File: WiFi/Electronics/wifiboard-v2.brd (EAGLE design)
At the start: 95.2 x 43.2 mm, 16 parts, among them IC2 7805DT, Q1 FDD8870, X1 MKDSN1,5/2-5,08, X2 MKDSN1,5/2-5,08

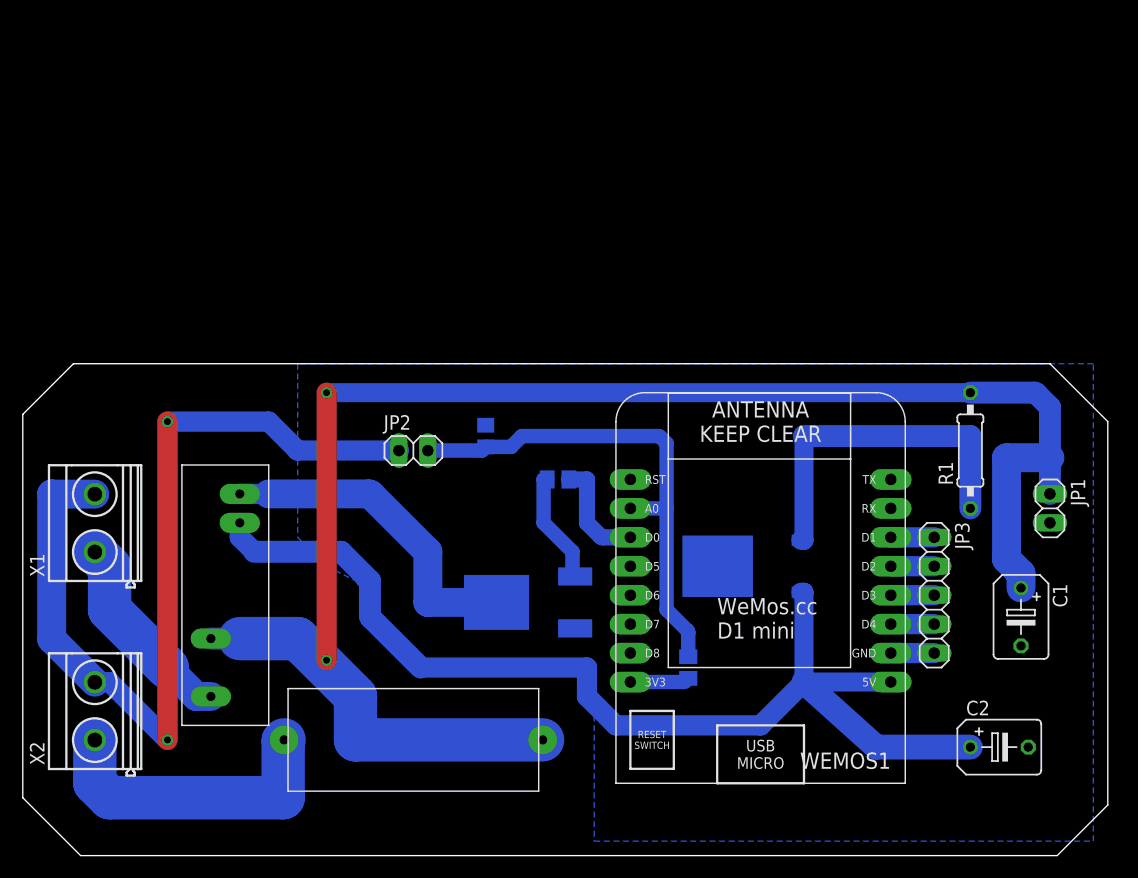
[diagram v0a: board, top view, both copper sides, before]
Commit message: heating.php improved to check that times monotonically increase throughout the day.
Various bits of experimental WiFi electronics added.
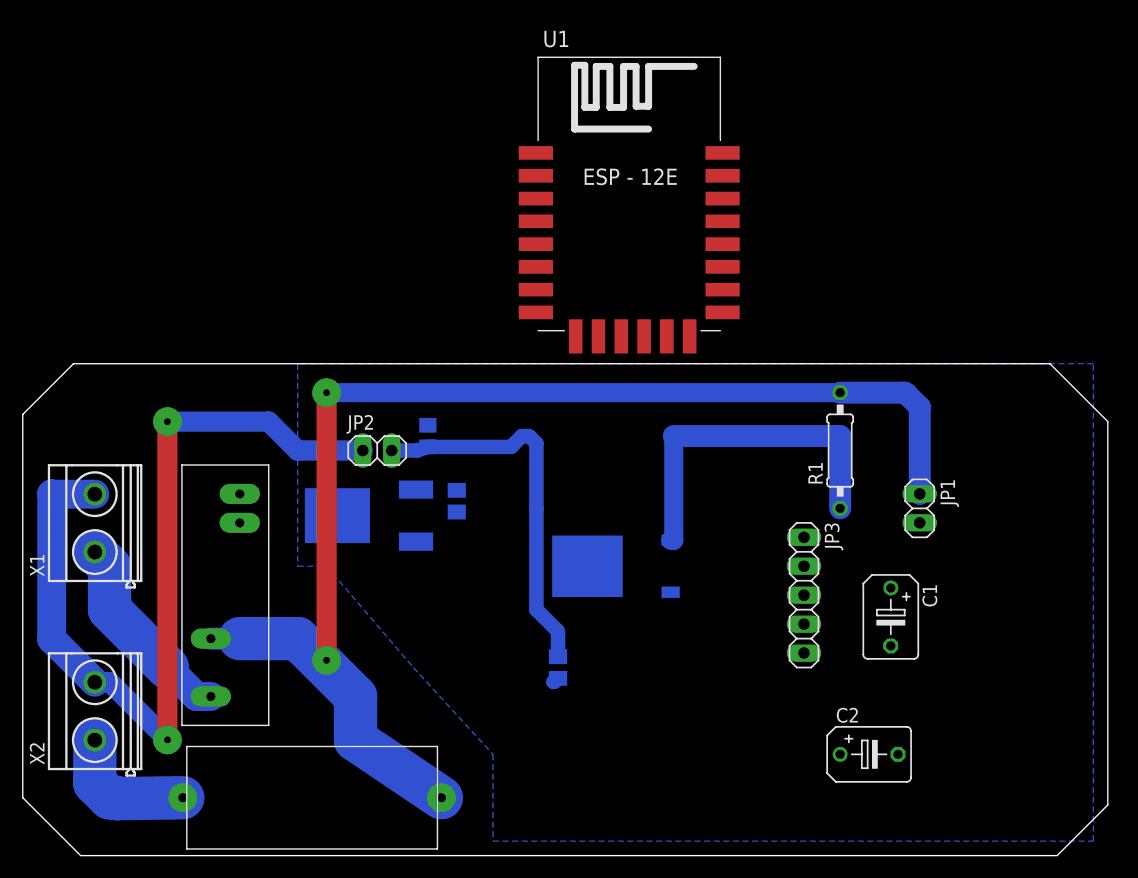
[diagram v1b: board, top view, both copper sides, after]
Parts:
- removed WEMOS1: (no value), esp8266modules:WEMOS-D1-MINI
- added U1: (no value), esp8266modules:ESP12E-SMD
- moved Q1 15.9 mm to (29.2, 28.6)
- moved C2 11.4 mm to (74.3, 7.62)
- moved JP1 11.4 mm to (78.7, 29.2)
- moved JP3 11.4 mm to (68.6, 21.6)
- moved R1 11.4 mm to (71.8, 34.3)
- moved IC2 11.4 mm to (52.1, 24.1)
- moved R2 11.4 mm to (47.0, 15.2)
- moved C1 11.4 mm to (76.2, 19.7)
- moved U$2 10.2 mm to (25.4, 3.81)
- moved R3 9.09 mm to (38.1, 29.8), turned to 270 degrees
- moved C3 5.08 mm to (35.6, 35.6)
- moved JP2 3.18 mm to (31.1, 34.3)
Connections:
- removed net N$11: JP3.4, WEMOS1.D4
- removed net N$13: JP3.3, WEMOS1.D3
- removed net N$14: JP3.2, WEMOS1.D2
- removed net N$15: JP3.1, WEMOS1.D1
- removed net N$3: C3.1, JP2.2, R2.2, WEMOS1.A0
- removed net N$4: R2.1, WEMOS1.3V3
- removed net N$6: R3.2, WEMOS1.D0
- new net +3V3: R2.1
- new net A0: C3.1, JP2.2, R2.2
- new net D0: R3.2
- new net D1: JP3.1
- new net D2: JP3.2
- new net D3: JP3.3
- new net D4: JP3.4
- net +12V: no longer C1.+
- net +5V: no longer WEMOS1.5V
- net GND: no longer WEMOS1.GND
- net N$2: now also C1.+
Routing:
- net +5V: track 95.1 -> 0.00 mm
- net N$3: track 44.4 -> 0.00 mm
- net +12V: track 148.4 -> 113.8 mm
- net A0: track 0.00 -> 32.9 mm
- net N$7: track 29.1 -> 0.00 mm
- net N$12: track 25.9 -> 12.1 mm
- net N$5: track 9.98 -> 0.00 mm
- net N$6: track 9.72 -> 0.00 mm
- net GND: track 83.5 -> 76.5 mm
- net N$4: track 5.20 -> 0.00 mm
- net N$15: track 3.81 -> 0.00 mm
- net N$14: track 3.81 -> 0.00 mm
- net N$13: track 3.81 -> 0.00 mm
- net N$11: track 3.81 -> 0.00 mm
- net +3V3: track 0.00 -> 0.54 mm

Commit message: Simple web monitoring added to the thermostat program.
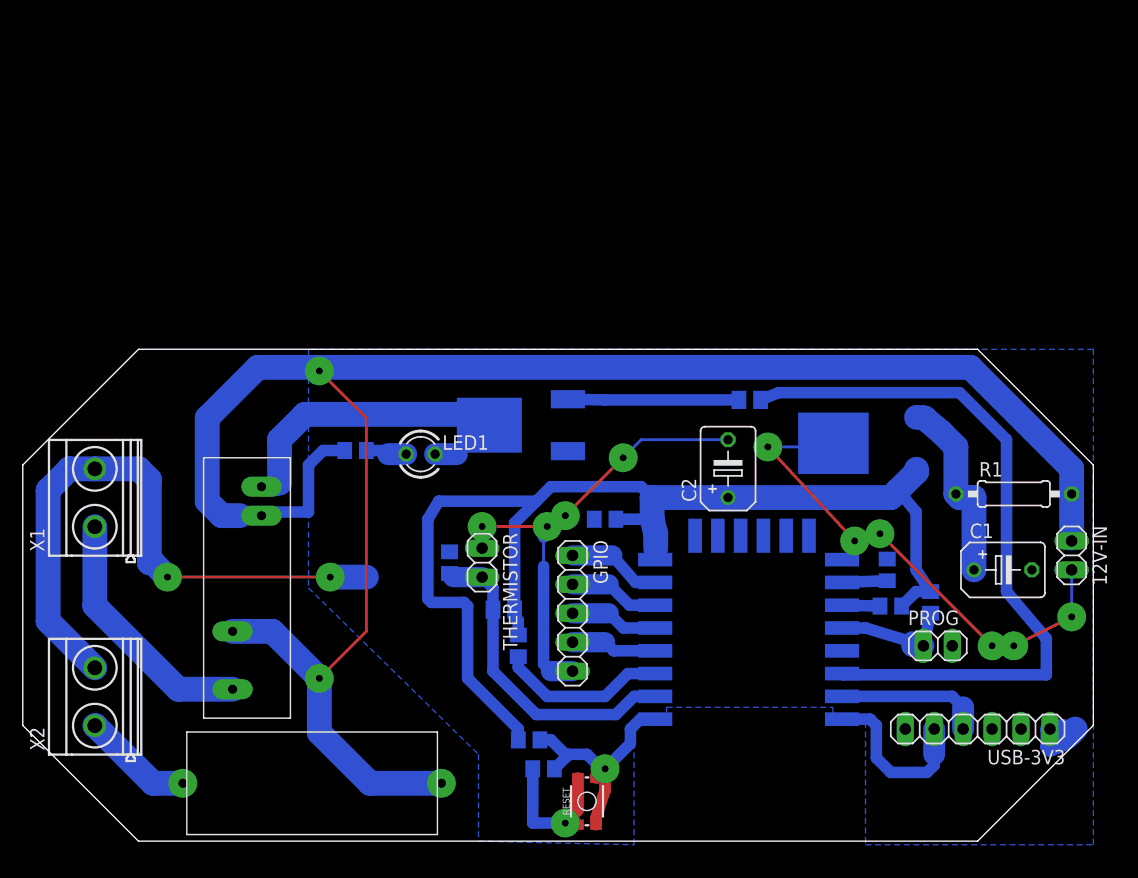
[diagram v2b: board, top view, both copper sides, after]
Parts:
- removed JP1, JP2: (no value), pinhead:1X02
- removed JP3: (no value), pinhead:1X05
- removed U$1: OMRON-G6DS, alexa:OMRON-G6DS-1A-H
- removed U$2: FUSE, alexa:FUSE
- removed U1: (no value), esp8266modules:ESP12E-SMD
- added 12V-IN, PROG, THERMISTOR: (no value), pinhead:1X02
- added C5, C6: 0.1u, rcl:C0805
- added FUSE: FUSE, alexa:FUSE
- added GPIO: (no value), pinhead:1X05
- added LED1: (no value), led:LED3MM
- added R4, R5, R6, R7, R8: 10K, rcl:R0805
- added R9: 1K, rcl:R0805
- added RELAY: OMRON-G6DS, alexa:OMRON-G6DS-1A-H
- added RESET: (no value), SparkFun-Switches:TACTILE_SWITCH_SMD_4.6X2.8MM
- added U2: (no value), esp8266modules:ESP12E-SMD
- added USB-3V3: (no value), pinhead:1X06
- IC2: value 7805DT -> 78033AF
- R1: value 27R -> 6R8
- R2: value 1K -> 10K
- X1: value MKDSN1,5/2-5,08 -> AC-N
- X2: value MKDSN1,5/2-5,08 -> AC-L
- moved C2 28.0 mm to (61.9, 32.7), turned to 90 degrees
- moved R3 27.2 mm to (63.8, 38.7), turned to 180 degrees
- moved IC2 24.1 mm to (73.7, 34.9)
- moved R1 15.7 mm to (87.0, 30.5), turned to 0 degrees
- moved Q1 15.5 mm to (42.5, 36.5)
- moved C3 11.3 mm to (37.5, 24.4)
- moved C1 10.7 mm to (86.0, 23.8), turned to 0 degrees
- moved R2 6.96 mm to (42.2, 20.3), turned to 0 degrees
- moved X1 2.22 mm to (6.35, 30.2)
- moved X2 1.27 mm to (6.35, 12.7)
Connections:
- removed net +5V: C2.+, IC2.2, U$1.P$2
- removed net D0: R3.2
- removed net D1: JP3.1
- removed net D2: JP3.2
- removed net D3: JP3.3
- removed net D4: JP3.4
- new net 0: PROG.1, R5.1, U2.GPIO0
- new net 12: GPIO.2, U2.GPIO12
- new net 13: GPIO.1, U2.GPIO13
- new net 14: GPIO.3, U2.GPIO14
- new net 15: R6.2, U2.GPIO15
- new net 16: GPIO.4, U2.GPIO16
- new net 2: R8.1, U2.GPIO2
- new net 5: R3.2, U2.GPIO5
- new net CH_PD: R7.1, U2.CH_PD
- new net N$14: LED1.A, R9.1
- new net RST: C6.1, R4.1, RESET.1, RESET.2, U2.RESET
- new net RX: U2.RXD0, USB-3V3.4
- new net TX: U2.TXD0, USB-3V3.5
- net +12V: now also 12V-IN.1, FUSE.P$1, R9.2, RELAY.P$2, RELAY.P$3; no longer JP1.1, U$1.P$3, U$2.P$1
- net +3V3: now also C2.+, C5.1, IC2.2, R4.2, R5.2, R7.2, R8.2, U2.VCC
- net A0: now also THERMISTOR.2, U2.ADC; no longer JP2.2
- net GND: now also 12V-IN.2, C5.2, C6.2, GPIO.5, PROG.2, R6.1, RESET.3, RESET.4, THERMISTOR.1, U2.GND, USB-3V3.1; no longer JP1.2, JP2.1, JP3.5
- net N$10: now also RELAY.P$4; no longer U$1.P$4
- net N$12: now also FUSE.P$2; no longer U$2.P$2
- net N$7: now also LED1.K, RELAY.P$1; no longer U$1.P$1
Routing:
- net +3V3: track 0.54 -> 104.6 mm
- net GND: track 76.5 -> 160.9 mm, vias 2 -> 13
- net 5: track 0.00 -> 63.3 mm
- net +12V: track 113.8 -> 169.9 mm
- net N$7: track 0.00 -> 31.5 mm
- net RST: track 0.00 -> 21.9 mm, vias 0 -> 1
- net TX: track 0.00 -> 15.1 mm
- net N$5: track 0.00 -> 15.0 mm
- net CH_PD: track 0.00 -> 14.9 mm
- net N$2: track 30.4 -> 16.6 mm
- net RX: track 0.00 -> 12.9 mm
- net 0: track 0.00 -> 10.6 mm
- net 13: track 0.00 -> 8.34 mm
- net 12: track 0.00 -> 8.02 mm
- net 14: track 0.00 -> 7.79 mm
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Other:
- board size 95.2 x 43.2 mm -> 94 x 43.2 mm
